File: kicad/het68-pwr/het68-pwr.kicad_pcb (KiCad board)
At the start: 2 copper layers, 90 x 50 mm, 19 parts, among them J1 AC_IN, J2 USB_C, J3 VSYS_OUT

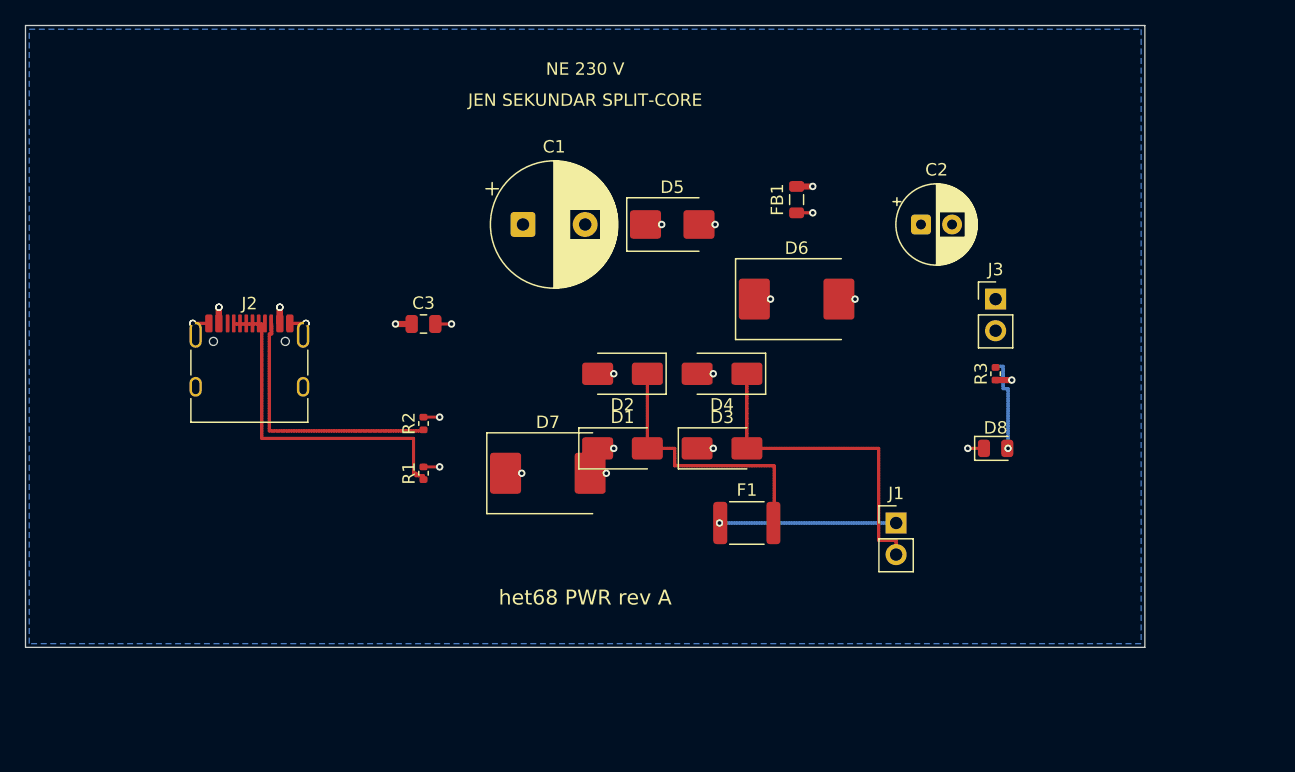
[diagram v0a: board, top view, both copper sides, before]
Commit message: Switch the boards to two layers and specify the power sources.
The HAT is no longer four-layer and the gerbers match that stackup. The power board now names the clamp CT, solar MPPT, 21700 cell and 5 V output; those charger parts are not drawn in KiCad yet.

Co-authored-by: Cursor <cursoragent@cursor.com>
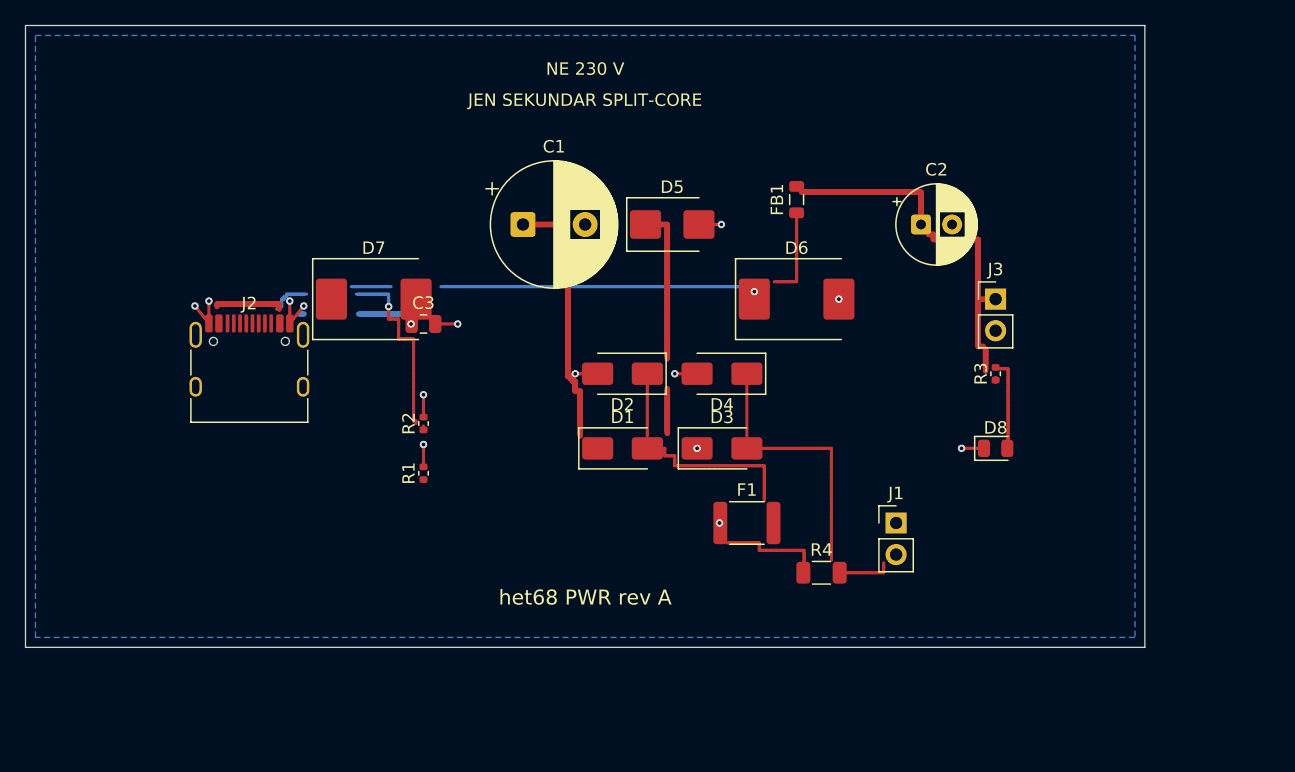
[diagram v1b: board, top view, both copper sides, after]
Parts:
- added R4: 100, R_1206_3216Metric, F.Cu at (64.0, 44.0)
- moved D7 19.8 mm to (28.0, 22.0)
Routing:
- net VSYS_RAW: track 3.90 -> 36.8 mm, vias 3 -> 1
- net DC: track 5.20 -> 37.8 mm, vias 4 -> 2
- net CC1: track 27.9 -> 0.00 mm
- net VSYS: track 2.60 -> 26.8 mm, vias 2 -> 0
- net AC1: track 14.3 -> 8.60 mm
- net GND: track 14.3 -> 19.8 mm
- net VBUS: track 7.80 -> 12.2 mm, vias 6 -> 1
- net AC1F: track 22.2 -> 18.6 mm
- net CC2: track 21.3 -> 19.2 mm, vias 0 -> 1
- net AC2: track 26.6 -> 25.2 mm
- net LED: track 7.66 -> 7.20 mm, vias 1 -> 0

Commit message: Reroute the two-layer boards and show the whole assembly.
The satellite now passes DRC, the power board no longer shorts, and the HAT parts sit beside the Pico instead of on it. Previews include the clamp on one mains conductor, the panel, the 21700 cell and the linked boards.

Co-authored-by: Cursor <cursoragent@cursor.com>
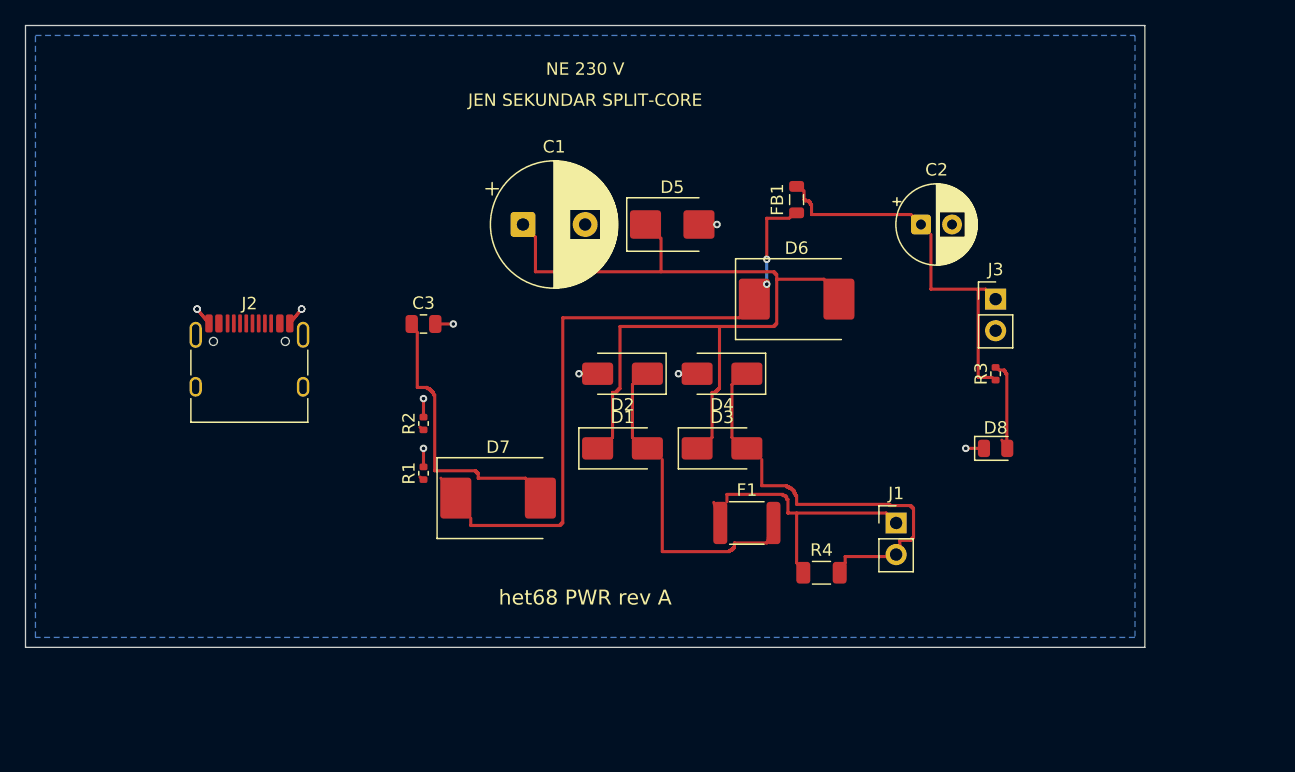
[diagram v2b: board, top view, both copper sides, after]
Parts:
- moved D7 18.9 mm to (38.0, 38.0)
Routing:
- net DC: track 37.8 -> 72.6 mm, vias 2 -> 0
- net CC2: track 19.2 -> 0.35 mm, vias 1 -> 0
- net AC1: track 8.60 -> 22.7 mm, vias 1 -> 0
- net VSYS_RAW: track 36.8 -> 50.6 mm, vias 1 -> 2
- net VBUS: track 12.2 -> 23.2 mm, vias 1 -> 0
- net AC2: track 25.2 -> 32.9 mm
- net AC1F: track 18.6 -> 25.3 mm
- net VSYS: track 26.8 -> 30.7 mm
- net GND: track 19.8 -> 16.3 mm

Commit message: Clear the remaining copper violations and add the order BOM.
HAT no longer reports shorts or clearance errors, and the power-board CC pins are connected. The order list now carries verified LCSC codes plus the power sources that are not drawn on the sheet yet.

Co-authored-by: Cursor <cursoragent@cursor.com>
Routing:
- net CC1: track 0.35 -> 38.9 mm
- net VBUS: track 23.2 -> 55.2 mm
- net CC2: track 0.35 -> 29.1 mm
- net GND: track 16.3 -> 25.9 mm
- net DC: track 72.6 -> 70.3 mm
- net VSYS_RAW: track 50.6 -> 49.0 mm
- net VSYS: track 30.7 -> 29.4 mm
- net AC2: track 32.9 -> 31.6 mm
- net AC1F: track 25.3 -> 24.2 mm
- net AC1: track 22.7 -> 21.7 mm
- net LED: track 7.34 -> 6.81 mm

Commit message: Shrink the acoustic board and ground the cable shield only at the HAT.
The HAT outline is 94 by 96 mm and the satellite shell pin is open. The README drops the power-board LED note and estimates a self-built Pico Plus 2 W against the bought module.

Co-authored-by: Cursor <cursoragent@cursor.com>
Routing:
- net VBUS: track 55.2 -> 50.4 mm

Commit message: Protect the CT secondary and ship clean power and satellite fab files.
Add burden, LC filter and crowbar on the power board, close DRC on power and satellite, and refresh the board previews for v1.10.0.

Co-authored-by: Cursor <cursoragent@cursor.com>
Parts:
- added C4: 1u/100V, C_1206_3216Metric, F.Cu at (58.0, 48.0)
- added L1: 470uH, L_Radial_D10.0mm_P5.00mm_Fastron_07P, F.Cu at (68.0, 42.0)
- added Q1: X0202MN, SOT-223, F.Cu at (52.0, 14.0)
- added R5: 1k, R_0805_2012Metric, F.Cu at (60.0, 14.0)
- C1: value 470u/25V -> 470u/50V
- D5: value SMBJ15A -> BZX84-C24; footprint D_SMB -> D_SOD-323
- R4: footprint R_1206_3216Metric -> R_Axial_DIN0207_L6.3mm_D2.5mm_P10.16mm_Horizontal
- moved J1 22.1 mm to (92.0, 42.0)
- moved R4 14.6 mm to (78.0, 48.0)
- moved C2 14.0 mm to (86.0, 16.0)
- moved D8 14.0 mm to (92.0, 34.0)
- moved FB1 14.0 mm to (76.0, 14.0)
- moved J3 14.0 mm to (92.0, 22.0)
- moved R3 14.0 mm to (92.0, 28.0)
- moved D5 8.94 mm to (60.0, 20.0)
- moved C3 8.25 mm to (24.0, 22.0)
- moved D6 8.25 mm to (70.0, 20.0)
- moved D7 7.21 mm to (32.0, 42.0)
- moved C1 6.00 mm to (34.0, 16.0)
- moved D1 2.00 mm to (48.0, 36.0)
- moved D2 2.00 mm to (48.0, 30.0)
- moved D3 2.00 mm to (56.0, 36.0)
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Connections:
- D5 pad 1: DC -> SCR_G
- F1 pad 1: AC1 -> AC1L
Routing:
- net VBUS: track 50.4 -> 79.5 mm
- net AC1L: track 0.00 -> 27.9 mm
- net AC2: track 31.6 -> 52.5 mm, vias 0 -> 3
- net VSYS_RAW: track 49.0 -> 69.1 mm, vias 2 -> 4
- net SCR_G: track 0.00 -> 19.9 mm
- net GND: track 25.9 -> 14.0 mm, vias 11 -> 12
- net AC1: track 21.7 -> 33.1 mm
- net AC1F: track 24.2 -> 17.7 mm
- net CC2: track 29.1 -> 27.9 mm, vias 0 -> 2
- net CC1: track 38.9 -> 37.7 mm, vias 0 -> 2
- net VSYS: track 29.4 -> 28.2 mm
- net DC: track 70.3 -> 69.3 mm, vias 0 -> 4
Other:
- board size 90 x 50 mm -> 100 x 58 mm
- board text added: "JEN SEKUNDAR CT"
- board text added: "NE 230 V / NE 22 kV"
- board text added: "burden+LC+crowbar ~25 V"
- board text added: "het68 PWR rev B"
- board text removed: "JEN SEKUNDAR SPLIT-CORE"
- board text removed: "NE 230 V"
- board text removed: "het68 PWR rev A"

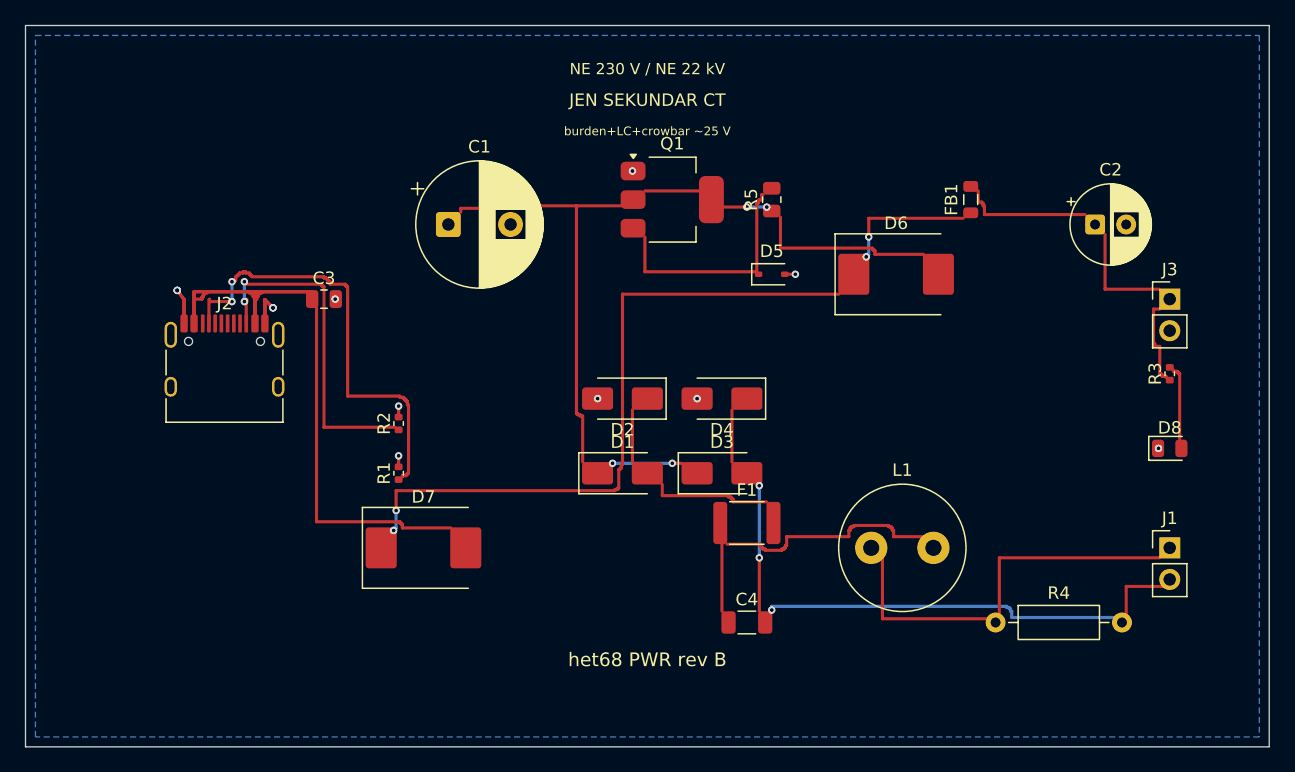
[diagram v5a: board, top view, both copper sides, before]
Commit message: Fit every board on printed.cz prototype: 2-layer, 0603, ENIG.
HAT is 140×140 mm so it routes on two layers without 0402 or BGA; satellite and power use the same stack, drill and finish.

Co-authored-by: Cursor <cursoragent@cursor.com>
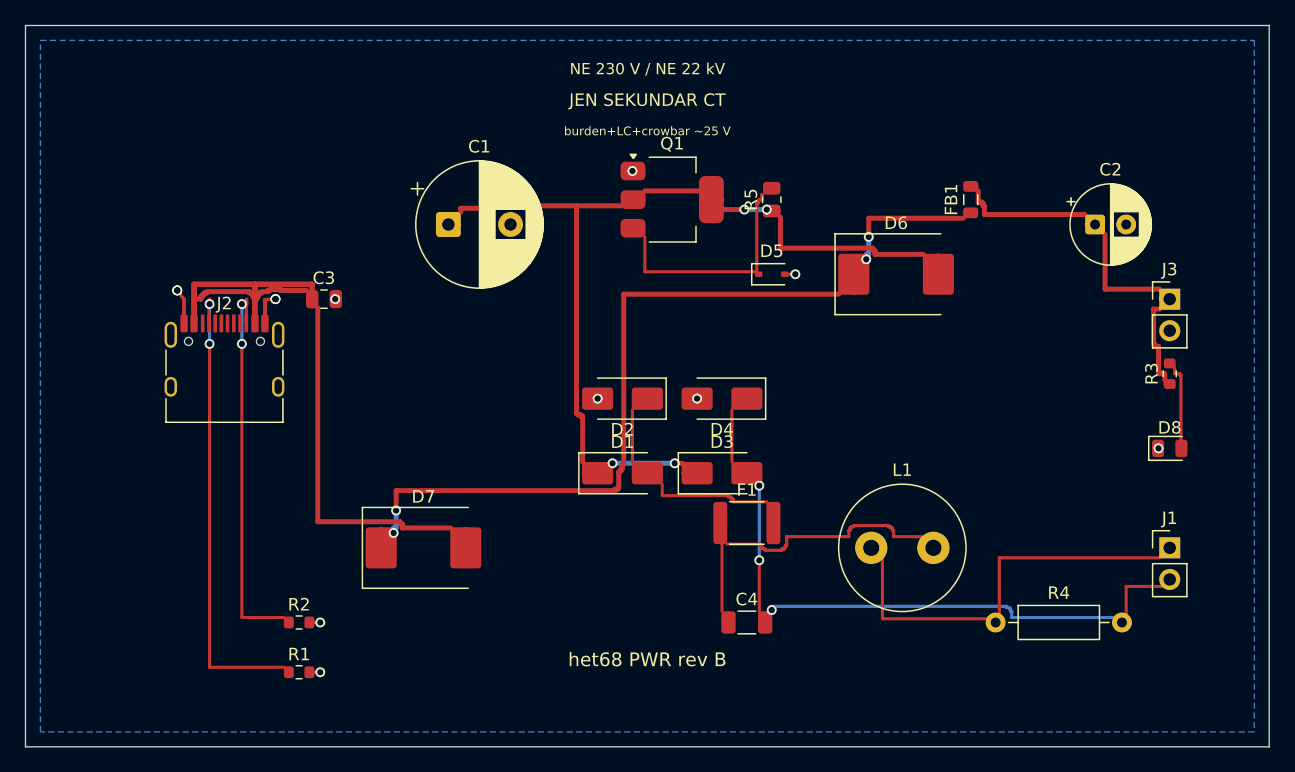
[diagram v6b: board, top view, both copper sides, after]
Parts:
- C1: footprint CP_Radial_D10.0mm_P5.00mm -> Capacitor_THT:CP_Radial_D10.0mm_P5.00mm
- C2: footprint CP_Radial_D6.3mm_P2.50mm -> Capacitor_THT:CP_Radial_D6.3mm_P2.50mm
- C3: footprint C_0805_2012Metric -> Capacitor_SMD:C_0805_2012Metric
- C4: footprint C_1206_3216Metric -> Capacitor_SMD:C_1206_3216Metric
- D1, D2, D3, D4: footprint D_SMA -> Diode_SMD:D_SMA
- D5: footprint D_SOD-323 -> Diode_SMD:D_SOD-323
- D6, D7: footprint D_SMC -> Diode_SMD:D_SMC
- D8: footprint LED_0805_2012Metric -> LED_SMD:LED_0805_2012Metric
- F1: footprint Fuse_1812_4532Metric -> Fuse:Fuse_1812_4532Metric
- FB1: footprint L_0805_2012Metric -> Inductor_SMD:L_0805_2012Metric
- J1, J3: footprint PinHeader_1x02_P2.54mm_Vertical -> Connector_PinHeader_2.54mm:PinHeader_1x02_P2.54mm_Vertical
- J2: footprint USB_C_Receptacle_HRO_TYPE-C-31-M-12 -> Connector_USB:USB_C_Receptacle_HRO_TYPE-C-31-M-12
- L1: footprint L_Radial_D10.0mm_P5.00mm_Fastron_07P -> Inductor_THT:L_Radial_D10.0mm_P5.00mm_Fastron_07P
- Q1: footprint SOT-223 -> Package_TO_SOT_SMD:SOT-223
- R1, R2, R3: footprint R_0402_1005Metric -> Resistor_SMD:R_0603_1608Metric
- R4: footprint R_Axial_DIN0207_L6.3mm_D2.5mm_P10.16mm_Horizontal -> Resistor_THT:R_Axial_DIN0207_L6.3mm_D2.5mm_P10.16mm_Horizontal
- R5: footprint R_0805_2012Metric -> Resistor_SMD:R_0805_2012Metric
- moved R1 17.9 mm to (22.0, 52.0), turned to 0 degrees
- moved R2 17.9 mm to (22.0, 48.0), turned to 0 degrees
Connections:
- J2 pad A6: (no net) -> unconnected-(J2-D+-PadA6)
- J2 pad A7: (no net) -> unconnected-(J2-D--PadA7)
- J2 pad A8: (no net) -> unconnected-(J2-SBU1-PadA8)
- J2 pad B6: (no net) -> unconnected-(J2-D+-PadB6)
- J2 pad B7: (no net) -> unconnected-(J2-D--PadB7)
- J2 pad B8: (no net) -> unconnected-(J2-SBU2-PadB8)
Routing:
- net VBUS: track 79.5 -> 83.5 mm
- net CC2: track 27.9 -> 31.6 mm
